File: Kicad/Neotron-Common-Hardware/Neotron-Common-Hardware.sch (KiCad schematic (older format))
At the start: 7 parts, among them J101 DB15_Female_HighDensity_Mount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, J102 AudioJack3, J103 DB9_Male_MountingHoles, J104 USB_B, J105 USB_A, J106 RJ45_Amphenol_RJMG1BD3B8K1ANR, J107 Double-mini-DIN-6

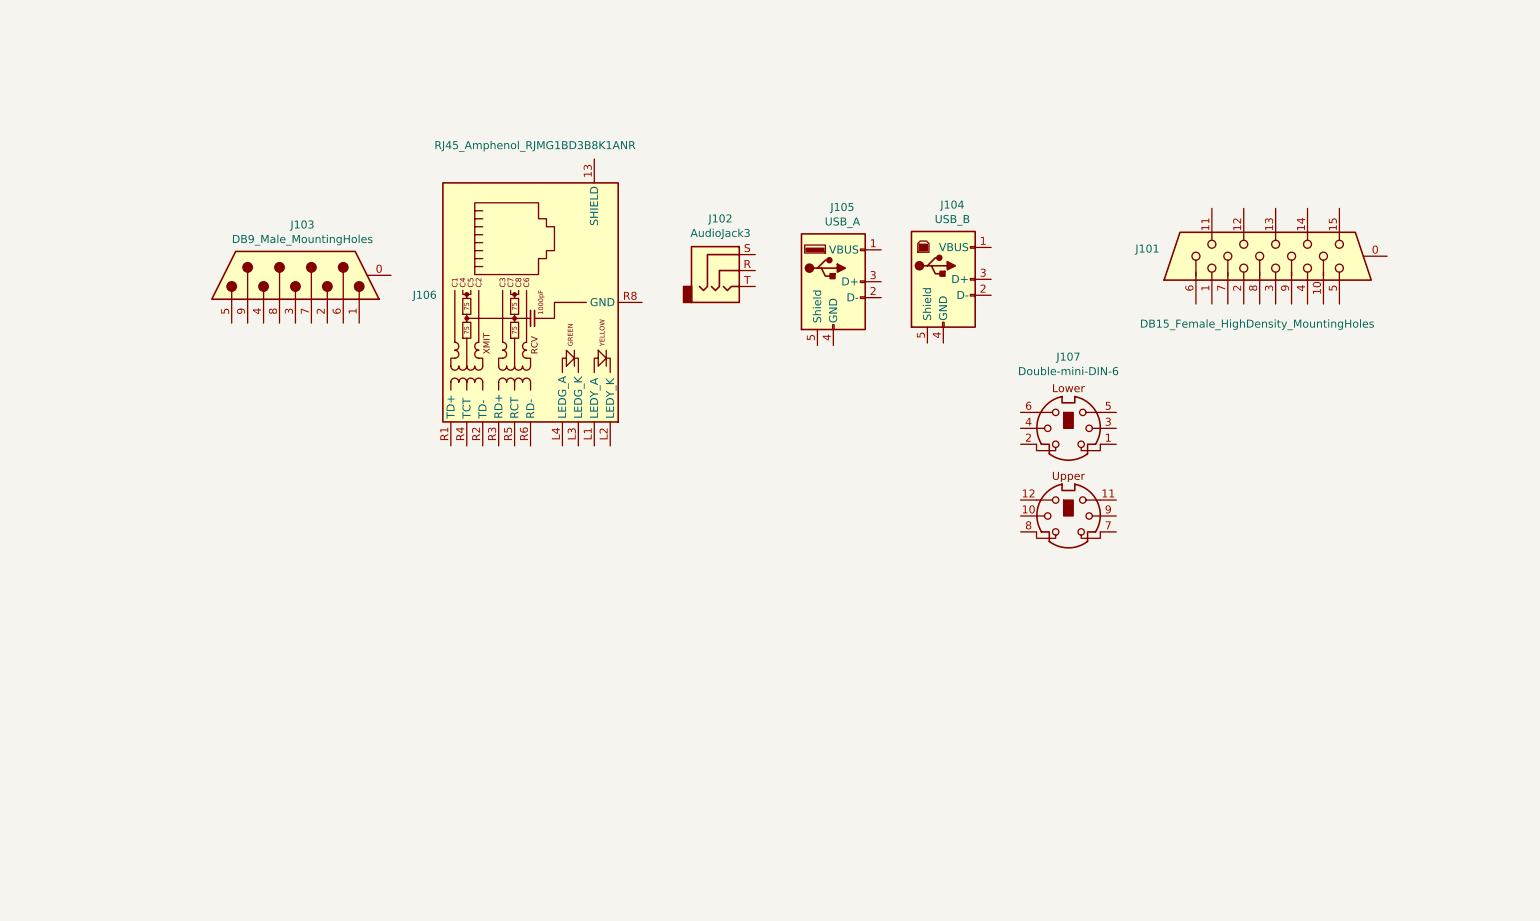
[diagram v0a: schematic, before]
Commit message: Add some comments to the schematic.
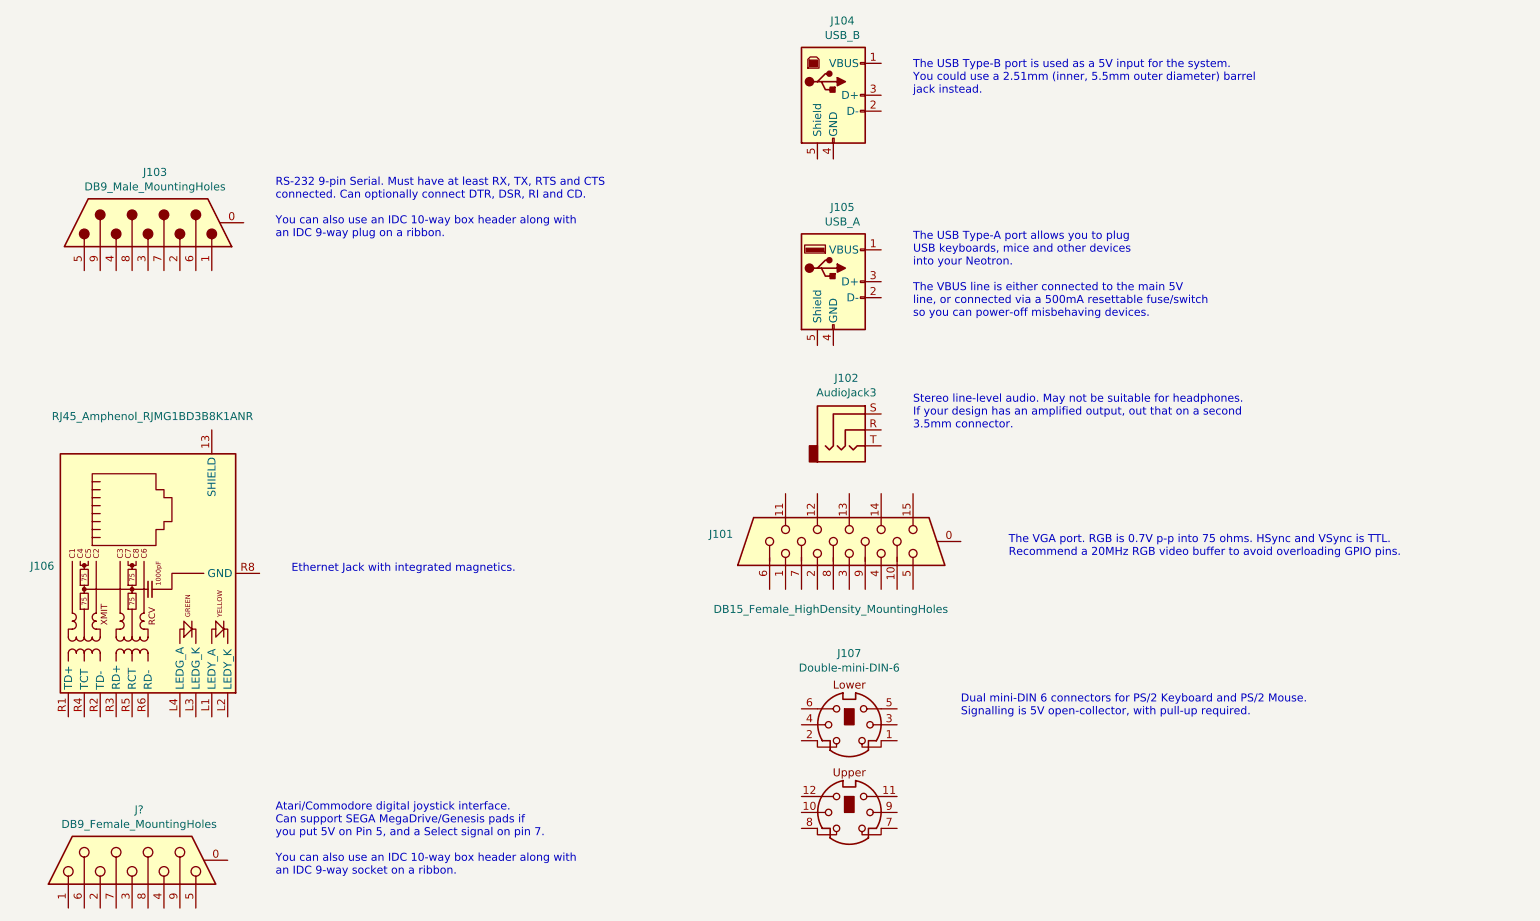
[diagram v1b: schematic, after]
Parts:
- added J?: DB9_Female_MountingHoles, symbol Connector:DB9_Female_MountingHoles
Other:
- note added: "Atari/Commodore digital joystick interface.\nCan support SEGA MegaDrive/Genesis pads if\nyou put 5V on Pin 5, and a Select signal on pin 7.\n\nYou can also use an IDC 10-way box header along with\nan IDC 9-way socket on a ribbon."
- note added: "Dual mini-DIN 6 connectors for PS/2 Keyboard and PS/2 Mouse.\nSignalling is 5V open-collector, with pull-up required."
- note added: "Ethernet Jack with integrated magnetics."
- note added: "RS-232 9-pin Serial. Must have at least RX, TX, RTS and CTS\nconnected. Can optionally connect DTR, DSR, RI and CD.\n\nYou can also use an IDC 10-way box header along with\nan IDC 9-way plug on a ribbon."
- note added: "Stereo line-level audio. May not be suitable for headphones.\nIf your design has an amplified output, out that on a second\n3.5mm connector."
- note added: "The USB Type-A port allows you to plug\nUSB keyboards, mice and other devices\ninto your Neotron.\n\nThe VBUS line is either connected to the main 5V\nline, or connected via a 500mA resettable fuse/switch\nso you can power-off misbehaving devices."
- note added: "The USB Type-B port is used as a 5V input for the system.\nYou could use a 2.51mm (inner, 5.5mm outer diameter) barrel\njack instead."
- note added: "The VGA port. RGB is 0.7V p-p into 75 ohms. HSync and VSync is TTL.\nRecommend a 20MHz RGB video buffer to avoid overloading GPIO pins."
- moved on the sheet: J101, J102, J103, J104, J106, J107
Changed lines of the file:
@@
 L Connector:DB9_Male_MountingHoles J103
 U 1 1 5FCBF65F
-P 2525 2430
-F 0 "J103" V 2842 2386 50  0000 C CNN
-F 1 "DB9_Male_MountingHoles" V 2751 2386 50  0000 C CNN
-F 2 "Connector_Dsub:DSUB-9_Male_Horizontal_P2.77x2.84mm_EdgePinOffset4.94mm_Housed_MountingHolesOffset7.48mm" H 2525 2430 50  0001 C CNN
-F 3 " ~" H 2525 2430 50  0001 C CNN
-	1    2525 2430
+P 1600 2100
+F 0 "J103" V 1917 2056 50  0000 C CNN
+F 1 "DB9_Male_MountingHoles" V 1826 2056 50  0000 C CNN
+F 2 "Connector_Dsub:DSUB-9_Male_Horizontal_P2.77x2.84mm_EdgePinOffset4.94mm_Housed_MountingHolesOffset7.48mm" H 1600 2100 50  0001 C CNN
+F 3 " ~" H 1600 2100 50  0001 C CNN
+	1    1600 2100
 	0    -1   -1   0
 $EndComp
@@
 L Connector:RJ45_Amphenol_RJMG1BD3B8K1ANR J106
 U 1 1 5FCC170E
-P 4000 2600
-F 0 "J106" V 4046 3188 50  0000 L CNN
-F 1 "RJ45_Amphenol_RJMG1BD3B8K1ANR" V 4985 1940 50  0000 L CNN
-F 2 "Connector_RJ:RJ45_Amphenol_RJMG1BD3B8K1ANR" H 4000 3300 50  0001 C CNN
-F 3 "https://www.amphenolcanada.com/ProductSearch/Drawings/AC/RJMG1BD3B8K1ANR.PDF" H 4000 3400 50  0001 C CNN
-	1    4000 2600
+P 1600 4300
+F 0 "J106" V 1646 4888 50  0000 L CNN
+F 1 "RJ45_Amphenol_RJMG1BD3B8K1ANR" V 2585 3640 50  0000 L CNN
+F 2 "Connector_RJ:RJ45_Amphenol_RJMG1BD3B8K1ANR" H 1600 5000 50  0001 C CNN
+F 3 "https://www.amphenolcanada.com/ProductSearch/Drawings/AC/RJMG1BD3B8K1ANR.PDF" H 1600 5100 50  0001 C CNN
+	1    1600 4300
 	0    -1   -1   0
 $EndComp
@@
 L Connector:AudioJack3 J102
 U 1 1 5FCC9839
-P 5210 2400
-F 0 "J102" H 5192 2725 50  0000 C CNN
-F 1 "AudioJack3" H 5192 2634 50  0000 C CNN
-F 2 "Connector_Audio:Jack_3.5mm_CUI_SJ1-3533NG_Horizontal" H 5210 2400 50  0001 C CNN
-F 3 "~" H 5210 2400 50  0001 C CNN
-	1    5210 2400
+P 6000 3400
+F 0 "J102" H 5982 3725 50  0000 C CNN
+F 1 "AudioJack3" H 5982 3634 50  0000 C CNN
+F 2 "Connector_Audio:Jack_3.5mm_CUI_SJ1-3533NG_Horizontal" H 6000 3400 50  0001 C CNN
+F 3 "~" H 6000 3400 50  0001 C CNN
+	1    6000 3400
 	1    0    0    -1
 $EndComp
@@
 L Connector:USB_B J104
 U 1 1 5FCCAB69
-P 6590 2455
-F 0 "J104" H 6647 2922 50  0000 C CNN
-F 1 "USB_B" H 6647 2831 50  0000 C CNN
-F 2 "Connector_USB:USB_B_OST_USB-B1HSxx_Horizontal" H 6740 2405 50  0001 C CNN
-F 3 " ~" H 6740 2405 50  0001 C CNN
-	1    6590 2455
+P 5900 1300
+F 0 "J104" H 5957 1767 50  0000 C CNN
+F 1 "USB_B" H 5957 1676 50  0000 C CNN
+F 2 "Connector_USB:USB_B_OST_USB-B1HSxx_Horizontal" H 6050 1250 50  0001 C CNN
+F 3 " ~" H 6050 1250 50  0001 C CNN
+	1    5900 1300
 	1    0    0    -1
 $EndComp
@@
 L Connector:DB15_Female_HighDensity_MountingHoles J101
 U 1 1 5FCCD62D
-P 8675 2310
-F 0 "J101" V 8721 3039 50  0000 L CNN
-F 1 "DB15_Female_HighDensity_MountingHoles" V 8250 1690 50  0000 L CNN
-F 2 "Connector_Dsub:DSUB-15-HD_Male_Horizontal_P2.29x1.98mm_EdgePinOffset3.03mm_Housed_MountingHolesOffset4.94mm" H 7725 2710 50  0001 C CNN
-F 3 " ~" H 7725 2710 50  0001 C CNN
-	1    8675 2310
+P 6000 4100
+F 0 "J101" V 6046 4829 50  0000 L CNN
+F 1 "DB15_Female_HighDensity_MountingHoles" V 5575 3480 50  0000 L CNN
+F 2 "Connector_Dsub:DSUB-15-HD_Male_Horizontal_P2.29x1.98mm_EdgePinOffset3.03mm_Housed_MountingHolesOffset4.94mm" H 5050 4500 50  0001 C CNN
+F 3 " ~" H 5050 4500 50  0001 C CNN
+	1    6000 4100
 	0    -1   -1   0
 $EndComp
@@
 L Neotron-Common-Hardware:Double-mini-DIN-6 J107
 U 1 1 5FCD0B49
-P 7375 3640
-F 0 "J107" H 7375 4338 50  0000 C CNN
-F 1 "Double-mini-DIN-6" H 7375 4247 50  0000 C CNN
-F 2 "Neotron-Common-Hardware:Double_mini-DIN_6" H 7375 3890 50  0001 C CNN
-F 3 "http://www.mouser.com/ds/2/18/40_c091_abd_e-75918.pdf" H 7375 3890 50  0001 C CNN
-	1    7375 3640
+P 6000 5500
+F 0 "J107" H 6000 6198 50  0000 C CNN
+F 1 "Double-mini-DIN-6" H 6000 6107 50  0000 C CNN
+F 2 "Neotron-Common-Hardware:Double_mini-DIN_6" H 6000 5750 50  0001 C CNN
+F 3 "http://www.mouser.com/ds/2/18/40_c091_abd_e-75918.pdf" H 6000 5750 50  0001 C CNN
+	1    6000 5500
 	1    0    0    -1
 $EndComp
+Text Notes 6400 2700 0    50   ~ 0
+The USB Type-A port allows you to plug\nUSB keyboards, mice and other devices\ninto your Neotron.\n\nThe VBUS line is either connected to the main 5V\nline, or connected via a 500mA resettable fuse/switch\nso you can power-off misbehaving devices.
+Text Notes 6400 1300 0    50   ~ 0
+The USB Type-B port is used as a 5V input for the system.\nYou could use a 2.51mm (inner, 5.5mm outer diameter) barrel\njack instead.
+Text Notes 6400 3400 0    50   ~ 0
+Stereo line-level audio. May not be suitable for headphones.\nIf your design has an amplified output, out that on a second\n3.5mm connector.
+Text Notes 7000 4200 0    50   ~ 0
+The VGA port. RGB is 0.7V p-p into 75 ohms. HSync and VSync is TTL.\nRecommend a 20MHz RGB video buffer to avoid overloading GPIO pins.
+Text Notes 6700 5200 0    50   ~ 0
+Dual mini-DIN 6 connectors for PS/2 Keyboard and PS/2 Mouse.\nSignalling is 5V open-collector, with pull-up required.
+Text Notes 2400 2200 0    50   ~ 0
+RS-232 9-pin Serial. Must have at least RX, TX, RTS and CTS\nconnected. Can optionally connect DTR, DSR, RI and CD.\n\nYou can also use an IDC 10-way box header along with\nan IDC 9-way plug on a ribbon.
+Text Notes 2500 4300 0    50   ~ 0
+Ethernet Jack with integrated magnetics.
+$Comp
+L Connector:DB9_Female_MountingHoles J?
+U 1 1 5FD5B463
+P 1500 6100
+F 0 "J?" V 1817 6056 50  0000 C CNN
+F 1 "DB9_Female_MountingHoles" V 1726 6056 50  0000 C CNN
+F 2 "" H 1500 6100 50  0001 C CNN
+F 3 " ~" H 1500 6100 50  0001 C CNN
+	1    1500 6100
+	0    -1   -1   0
+$EndComp
+Text Notes 2400 6200 0    50   ~ 0
+Atari/Commodore digital joystick interface.\nCan support SEGA MegaDrive/Genesis pads if\nyou put 5V on Pin 5, and a Select signal on pin 7.\n\nYou can also use an IDC 10-way box header along with\nan IDC 9-way socket on a ribbon.
 $EndSCHEMATC
